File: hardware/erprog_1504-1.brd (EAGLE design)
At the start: 57.8 x 21.6 mm, 41 parts, among them IC1 ISO7231MDW, IC2 FT4232HL, IC4 TPS76133, IC5 ISO7231MDW, Q2 12MHz, X1 JTAG, X2 USB-SHIELD-MINI-B-BUCHSE-R-AS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

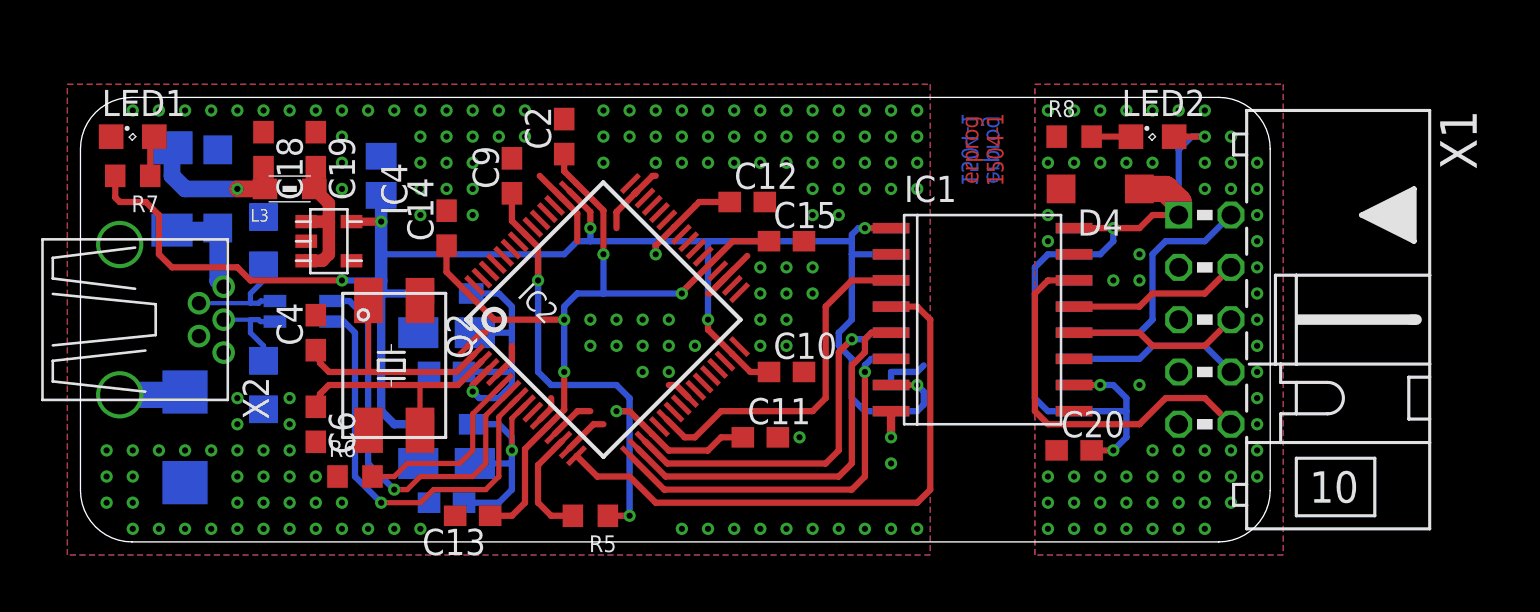
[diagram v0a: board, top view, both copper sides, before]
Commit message: rearranged names of parts
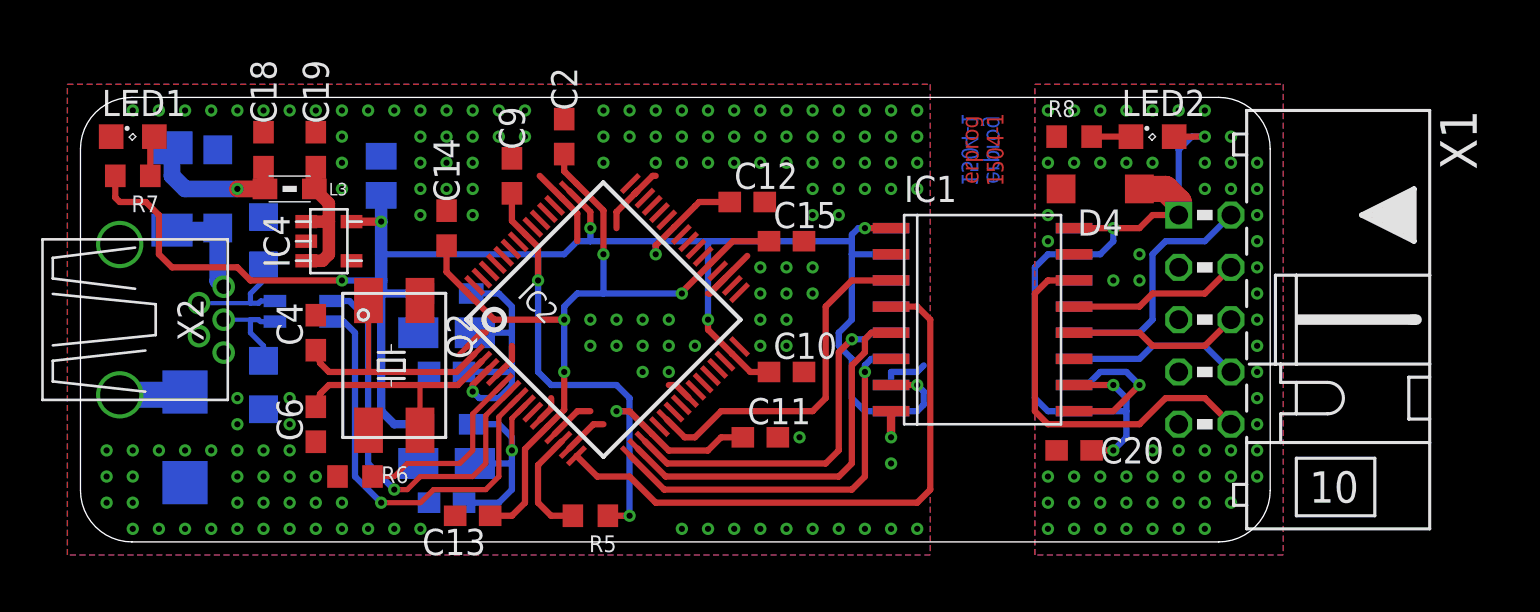
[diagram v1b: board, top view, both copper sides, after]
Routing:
- net GND_EXT: track 0.00 -> 7.40 mm
